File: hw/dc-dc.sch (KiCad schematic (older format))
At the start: 8 parts

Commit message: hw: add mounting holes
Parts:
- VD1: footprint (none) -> hat:D-PowerDI-5
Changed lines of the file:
@@
 F 0 "VD1" V 5304 6029 50  0000 L CNN
 F 1 "PDS760-13" V 5395 6029 50  0000 L CNN
-F 2 "" H 5350 5950 50  0001 C CNN
+F 2 "hat:D-PowerDI-5" H 5350 5950 50  0001 C CNN
 F 3 "~" H 5350 5950 50  0001 C CNN
 	1    5350 5950

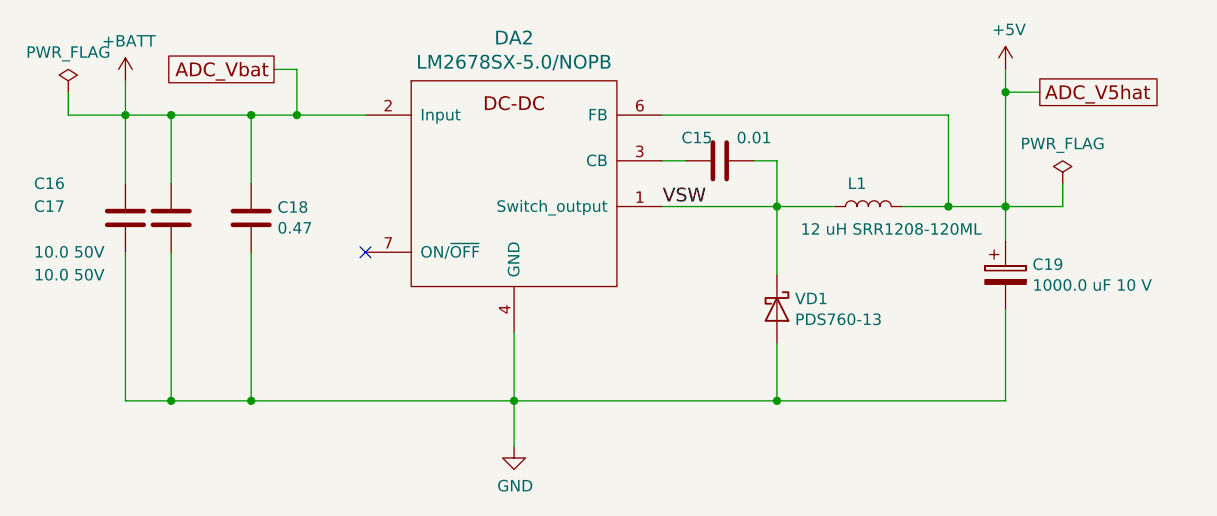
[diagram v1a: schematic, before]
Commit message: hw: add battery input connector
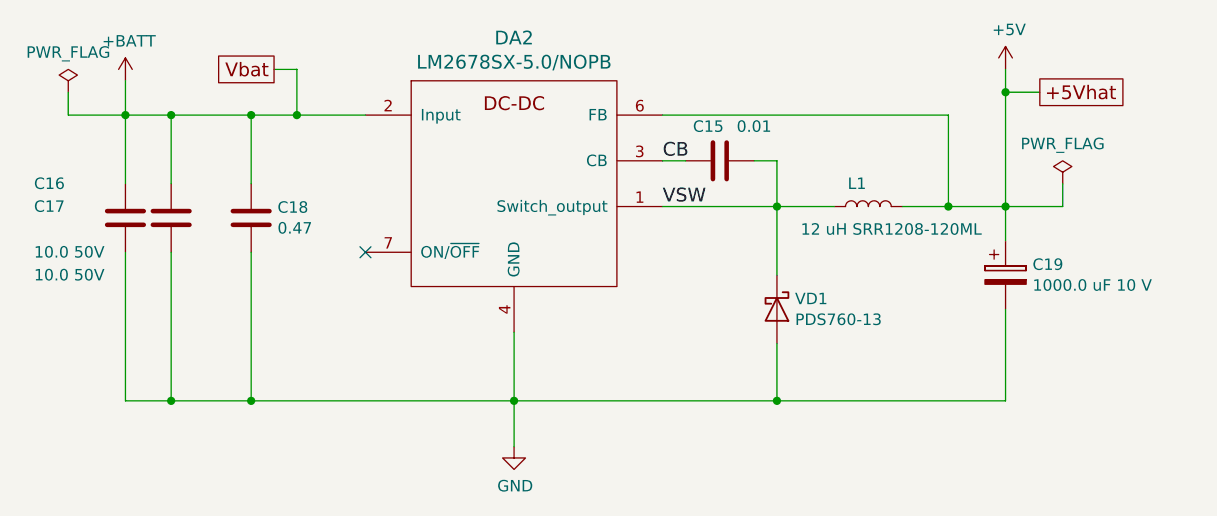
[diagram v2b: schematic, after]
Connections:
- net CB: now reaches C15.2, DA2.3 (CB)
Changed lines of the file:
@@
 $EndDescr
 Text GLabel 3150 4900 0    60   UnSpc ~ 0
-ADC_Vbat
+Vbat
 Text GLabel 6500 5000 2    60   UnSpc ~ 0
-ADC_V5hat
++5Vhat
 $Comp
 L power:+BATT #PWR060
@@
 U 1 1 5AD6310A
 P 5100 5300
-F 0 "C15" V 5000 5200 50  0000 C CNN
-F 1 "0.01" V 5000 5450 50  0000 C CNN
+F 0 "C15" V 4950 5250 50  0000 C CNN
+F 1 "0.01" V 4950 5450 50  0000 C CNN
 F 2 "Capacitor_SMD:C_0603_1608Metric" H 5138 5150 50  0001 C CNN
 F 3 "~" H 5100 5300 50  0001 C CNN
@@
 Wire Wire Line
 	2700 6350 3050 6350
+Text Label 4850 5300 0    60   ~ 0
+CB
 $EndSCHEMATC
